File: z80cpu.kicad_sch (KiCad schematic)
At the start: 9 parts

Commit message: Notes and minor fixes
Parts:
- gave numbers to parts that had none: 1
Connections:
- net ~{RFSH}: now reaches F6.14 (O2a)
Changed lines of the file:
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@@
+    (stroke (width 0) (type default))
+  )
+  (wire (pts (xy 39.37 81.28) (xy 46.99 81.28))
     (stroke (width 0) (type default))
   )
@@
   (label "~{RD}" (at 30.48 123.19 180) (fields_autoplaced)
     (effects (font (size 1.27 1.27)) (justify right bottom))
+  )
+  (label "~{RFSH}" (at 39.37 81.28 0) (fields_autoplaced)
+    (effects (font (size 1.27 1.27)) (justify left bottom))
   )
   (label "~{m1}" (at 80.01 91.44 180) (fields_autoplaced)
@@
   (symbol (lib_id "74xx:74LS244") (at 198.12 41.91 0) (unit 1)
     (in_bom yes) (on_board yes) (dnp no) (fields_autoplaced)
-    (property "Reference" "U?" (at 200.1394 21.59 0)
+    (property "Reference" "H3" (at 200.0759 22.86 0)
       (effects (font (size 1.27 1.27)) (justify left))
     )
-    (property "Value" "74LS244" (at 200.1394 24.13 0)
+    (property "Value" "74LS244" (at 200.0759 25.4 0)
       (effects (font (size 1.27 1.27)) (justify left))
     )
@@
       (project "ceda"
         (path "/12a6dbe3-008d-4c5b-88f6-9f1c816060be/1847fdc4-53d8-4940-8c5f-7a326599bae2"
-          (reference "U?") (unit 1)
-        )
-      )
+          (reference "H3") (unit 1)
+        )
+      )

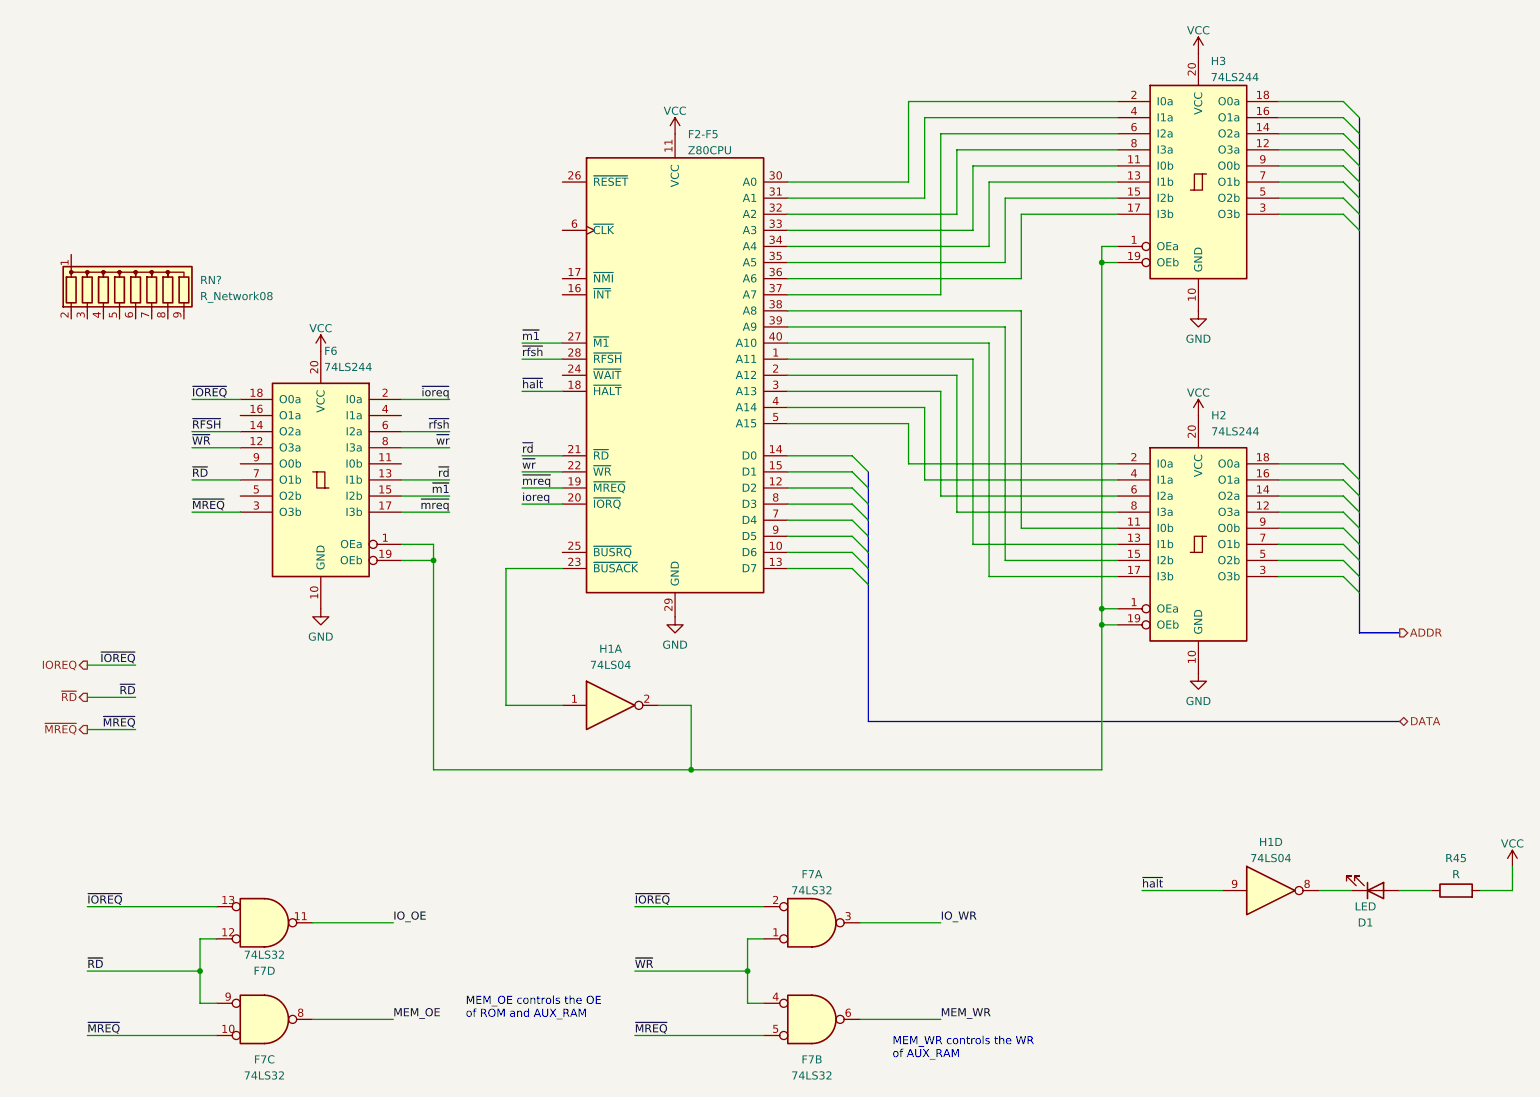
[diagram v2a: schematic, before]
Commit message: Z80 and reset/clock: wire naming
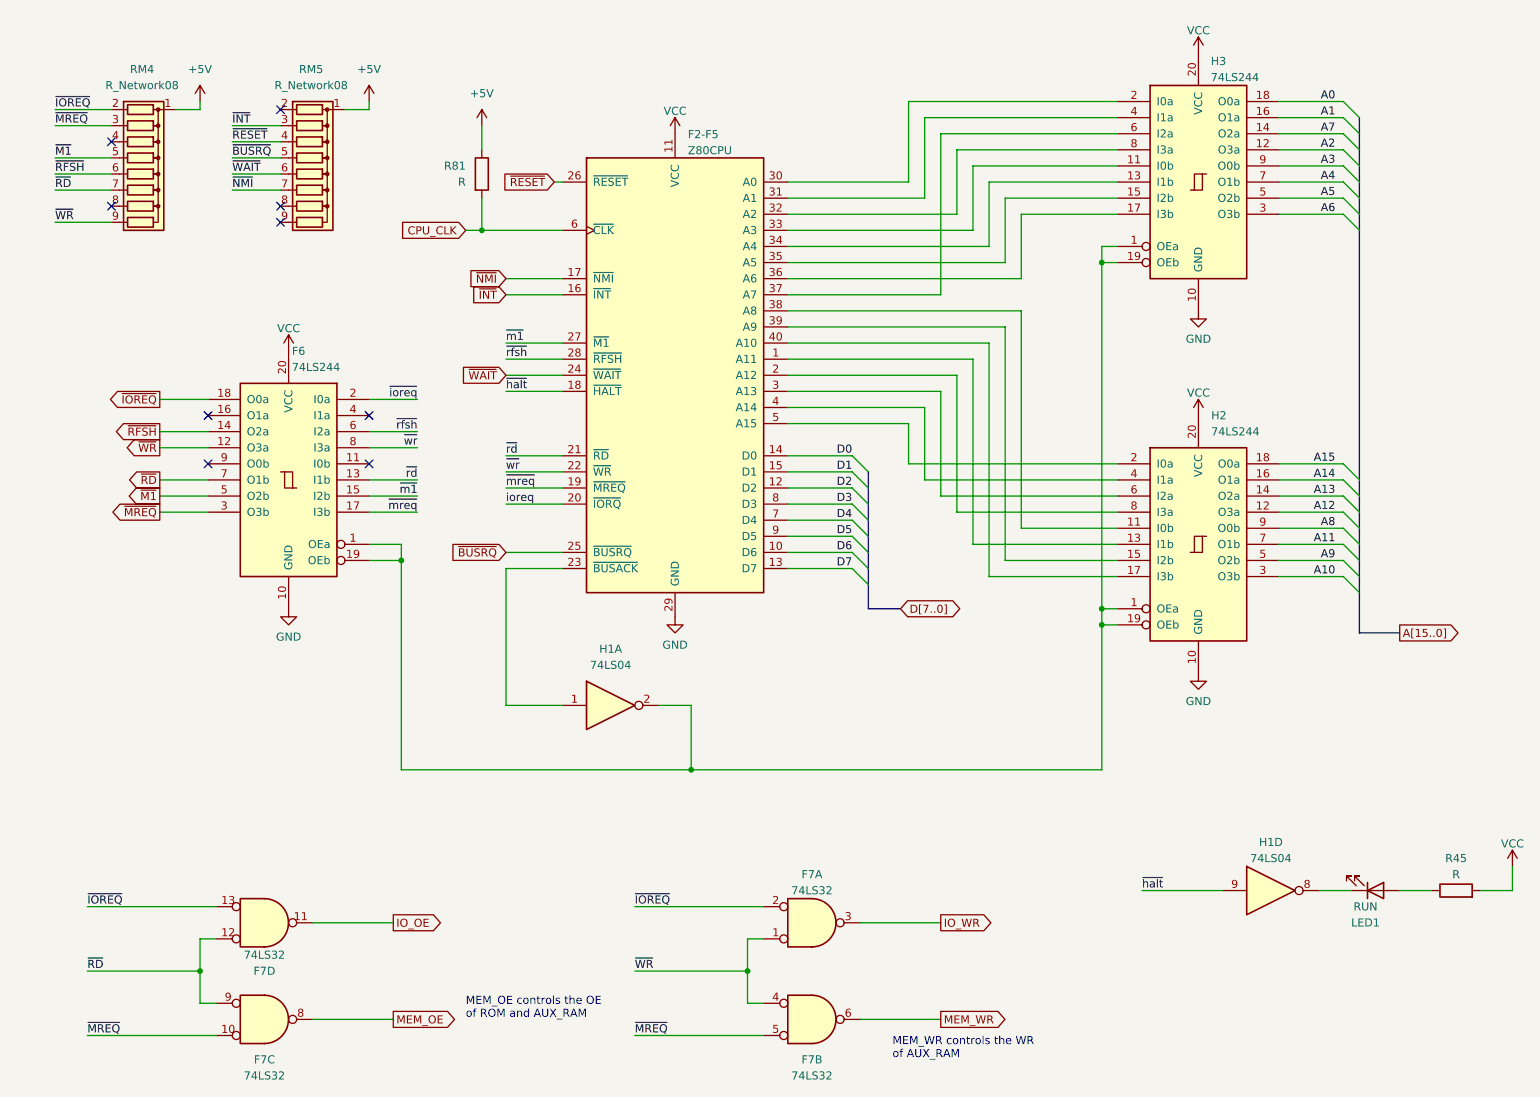
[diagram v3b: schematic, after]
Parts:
- added R81: R, symbol Device:R
- added RM5: R_Network08, Resistor_THT:R_Array_SIP9, symbol Device:R_Network08
- LED1: renamed from D1; value LED -> RUN
- gave numbers to parts that had none: 1
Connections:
- net IOREQ is gone; now on net ~{IOREQ}: F6.18 (O0a), F7.13, F7.2
- net ~{MREQ}: now also RM4.3 (R2)
- net ~{RD}: now also RM4.7 (R6)
- net ~{RFSH}: now also RM4.6 (R5)
- net ~{WR}: now also RM4.9 (R8)
- net +5V: now reaches RM4.1 (common)
- net +5V: now also R81.1, RM5.1 (common)
- net ~{IOREQ}: now reaches RM4.2 (R1)
- net ~{M1}: now reaches RM4.5 (R4)
- net ~{M1}: now also F6.5 (O2b)
- net A2: now reaches H3.12 (O3a)
- net A7: now reaches H3.14 (O2a)
- net A1: now reaches H3.16 (O1a)
- net A0: now reaches H3.18 (O0a)
- net A6: now reaches H3.3 (O3b)
- net A5: now reaches H3.5 (O2b)
- net A4: now reaches H3.7 (O1b)
- net A3: now reaches H3.9 (O0b)
- net D6: now reaches F2-F5.10 (D6)
- net D2: now reaches F2-F5.12 (D2)
- net D7: now reaches F2-F5.13 (D7)
- net D0: now reaches F2-F5.14 (D0)
- net D1: now reaches F2-F5.15 (D1)
- net ~{INT}: now reaches F2-F5.16 (~{INT})
- net ~{INT}: now also RM5.3 (R2)
- net ~{NMI}: now reaches F2-F5.17 (~{NMI})
- net ~{NMI}: now also RM5.7 (R6)
- net ~{WAIT}: now reaches F2-F5.24 (~{WAIT})
- net ~{WAIT}: now also RM5.6 (R5)
- net ~{BUSRQ}: now reaches F2-F5.25 (~{BUSRQ})
- net ~{BUSRQ}: now also RM5.5 (R4)
- net ~{RESET}: now reaches F2-F5.26 (~{RESET})
- net ~{RESET}: now also RM5.4 (R3)
- net CPU_CLK: now reaches F2-F5.6 (~{CLK})
- net CPU_CLK: now also R81.2
- net D4: now reaches F2-F5.7 (D4)
- net D3: now reaches F2-F5.8 (D3)
- net D5: now reaches F2-F5.9 (D5)
- net A12: now reaches H2.12 (O3a)
- net A13: now reaches H2.14 (O2a)
- net A14: now reaches H2.16 (O1a)
- net A15: now reaches H2.18 (O0a)
- net A10: now reaches H2.3 (O3b)
- net A9: now reaches H2.5 (O2b)
- net A11: now reaches H2.7 (O1b)
- net A8: now reaches H2.9 (O0b)
- no-connect marks 0 -> 9
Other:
- moved on the sheet: F6, RM4
